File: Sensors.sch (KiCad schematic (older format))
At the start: 52 parts, among them CON1 CONSOLE, P1 CONN_02X20, P10 CBUS, P11 I2C0, P12 I2C1, P13 I2C1, P14 I2C1, P7 96B_SPI, U1 CJT1117-3.3, U2 XC6206, U3 FT230XS, U4 TXB0108PW, U5 TXS0108E, U6 PCA9306, U7 PCA9306

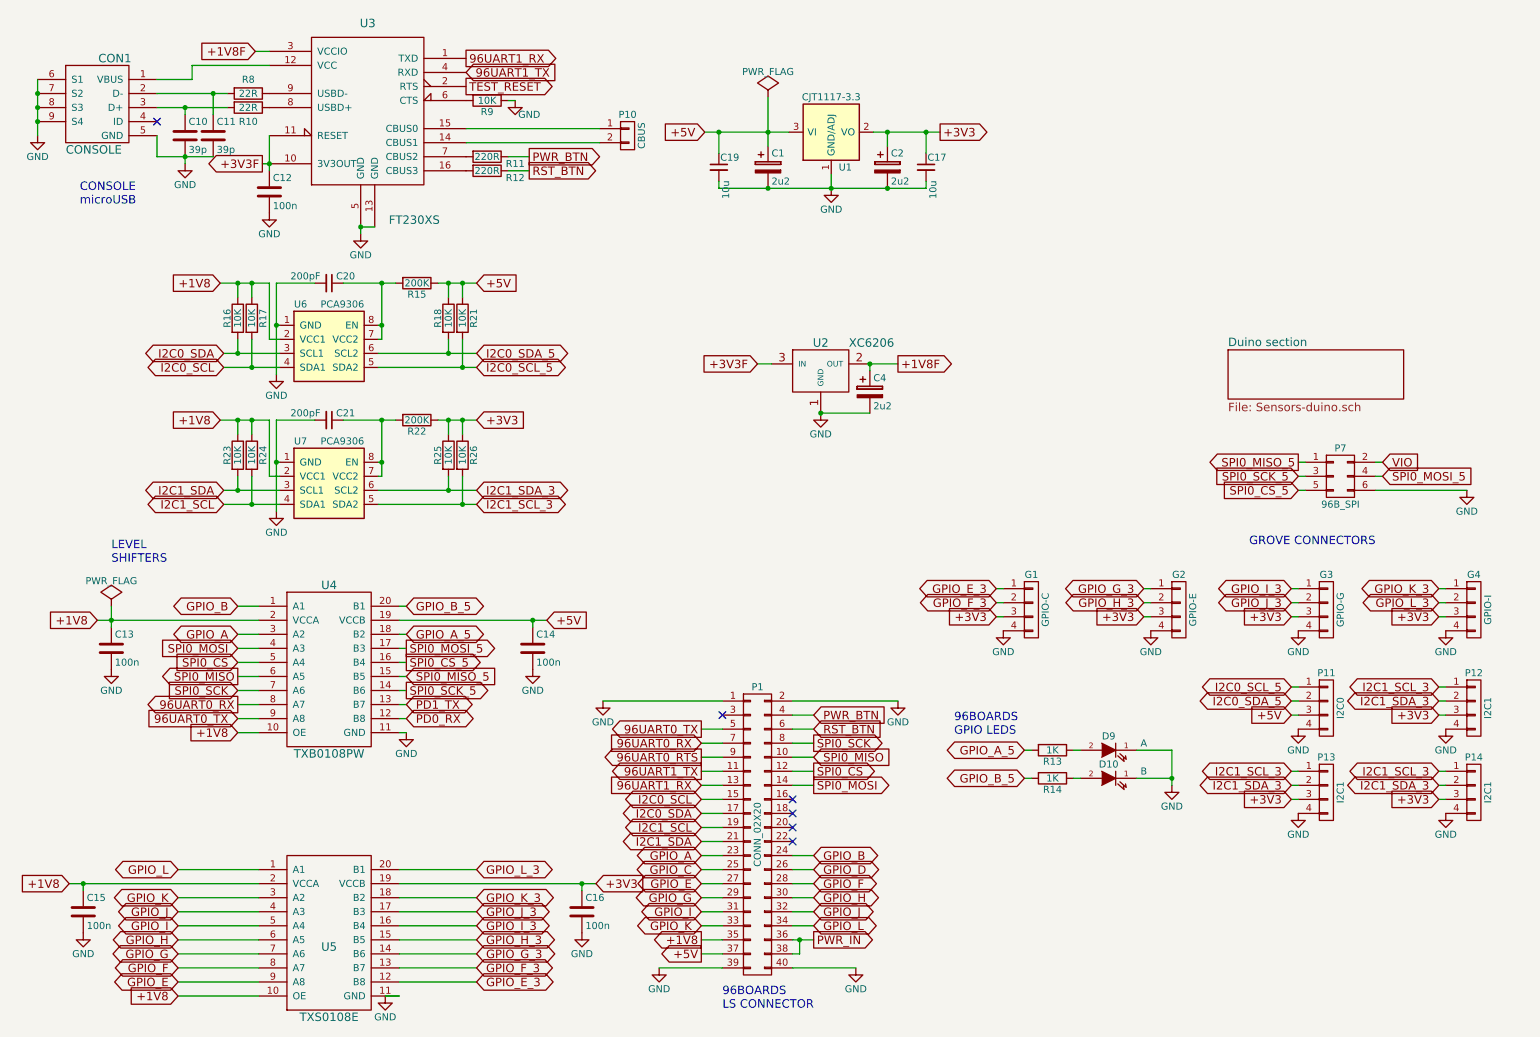
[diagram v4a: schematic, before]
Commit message: Fix missing caps on FT230X power supply
The USB power rail decoupling caps were missing for the FT230X part. Add
them back in.

Signed-off-by: Grant Likely <grant.likely@linaro.org>
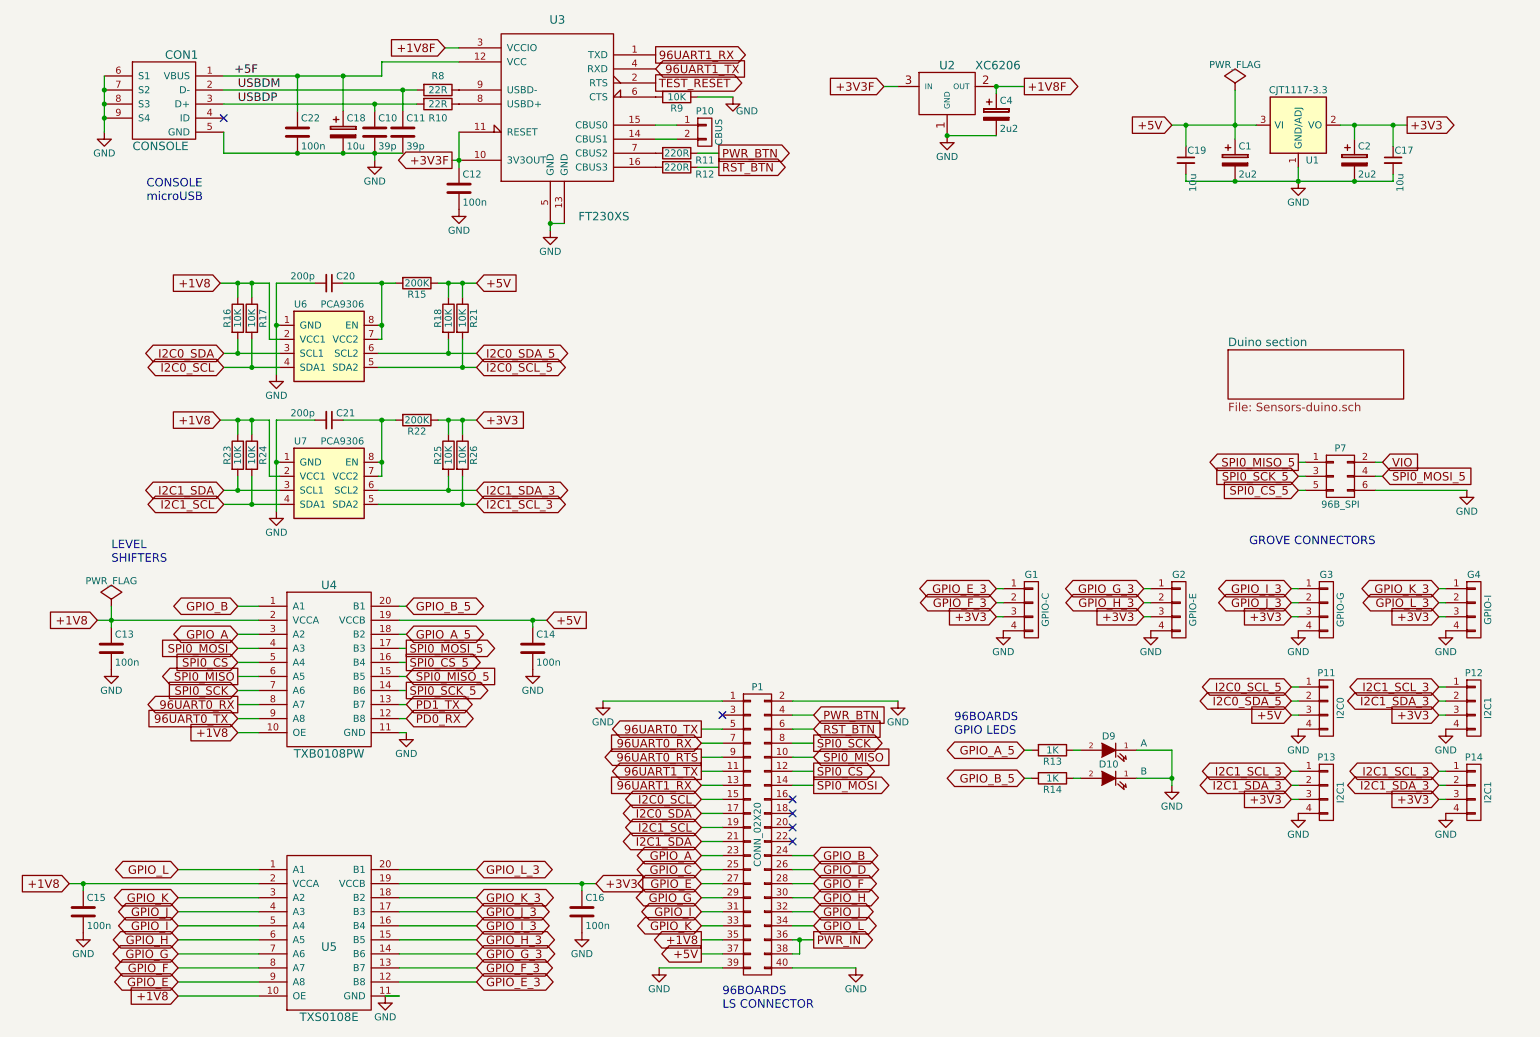
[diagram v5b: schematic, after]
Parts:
- added C18: 10u, Capacitors_SMD:C_0805, symbol CP
- added C22: 100n, Capacitors_SMD:C_0603, symbol C
- C20, C21: value 200pF -> 200p
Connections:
- net GND: now also C18.2, C22.2
- net +5F: now reaches CON1.1 (VBUS), U3.12 (VCC)
- net +5F: now also C18.1, C22.1
- net USBDM: now reaches C11.1, CON1.2 (D-), R8.2
- net USBDP: now reaches C10.1, CON1.3 (D+), R10.2
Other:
- moved on the sheet: C1, C10, C11, C12, C17, C19, C2, C4, CON1, P10, R10, R11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

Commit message: Update component part numbers
Make sure the correct part numbers are in the schematic for generating a
BOM.

Signed-off-by: Grant Likely <grant.likely@linaro.org>
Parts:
- C18: Mfr Part # CC0805KKX7R8BB225 -> CC0805KKX5R8BB106; Seeed SKU 302010148 -> 302010178
- C19: Mfr YAGEO -> Yageo
- C20, C21: value 200p -> 100p; Mfr (none) -> Yageo; Mfr Part # (none) -> CC0603JRNPO9BN101; Seeed SKU (none) -> 302010076
- C22: renamed from C17; Mfr YAGEO -> Yageo
- G1: value GPIO-C -> GROVE
- G2: value GPIO-E -> GROVE
- G3: value GPIO-G -> GROVE
- G4: value GPIO-I -> GROVE
- I2C0: renamed from P11; value I2C0 -> GROVE
- I2C1: renamed from P12; value I2C1 -> GROVE
- R15, R22: Mfr (none) -> Yageo; Mfr Part # (none) -> RC0603JR-07200KL; Seeed SKU (none) -> 301010212
- R16, R17, R18, R21, R23, R24, R25, R26: Mfr (none) -> Yageo; Mfr Part # (none) -> RC0603FR-0710KL; Seeed SKU (none) -> 301010299
- U6, U7: Mfr (none) -> TI; Mfr Part # (none) -> PCA9306DCU
- renumbered C22 to C17
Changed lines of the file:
@@
 $EndComp
 $Comp
-L CONN_01X04 P11
+L CONN_01X04 I2C0
 U 1 1 55BC070F
 P 9850 5550
-F 0 "P11" H 9850 5800 50  0000 C CNN
-F 1 "I2C0" V 9950 5550 50  0000 C CNN
+F 0 "I2C0" H 9850 5800 50  0000 C CNN
+F 1 "GROVE" V 9950 5550 50  0000 C CNN
 F 2 "Sensors:Grove_SMD_Connector" H 9850 5550 60  0001 C CNN
 F 3 "" H 9850 5550 60  0000 C CNN
@@
 $EndComp
 $Comp
-L CONN_01X04 P12
+L CONN_01X04 I2C1
 U 1 1 55BC07A4
 P 10900 5550
-F 0 "P12" H 10900 5800 50  0000 C CNN
-F 1 "I2C1" V 11000 5550 50  0000 C CNN
+F 0 "I2C1" H 10900 5800 50  0000 C CNN
+F 1 "GROVE" V 11000 5550 50  0000 C CNN
 F 2 "Sensors:Grove4P" H 10900 5550 60  0001 C CNN
 F 3 "" H 10900 5550 60  0000 C CNN
@@
 P 9850 4850
 F 0 "G3" H 9850 5100 50  0000 C CNN
-F 1 "GPIO-G" V 9950 4850 50  0000 C CNN
+F 1 "GROVE" V 9950 4850 50  0000 C CNN
 F 2 "Sensors:Grove4P" H 9850 4850 60  0001 C CNN
 F 3 "" H 9850 4850 60  0000 C CNN
@@
 P 8800 4850
 F 0 "G2" H 8800 5100 50  0000 C CNN
-F 1 "GPIO-E" V 8900 4850 50  0000 C CNN
+F 1 "GROVE" V 8900 4850 50  0000 C CNN
 F 2 "Sensors:Grove4P" H 8800 4850 60  0001 C CNN
 F 3 "" H 8800 4850 60  0000 C CNN
@@
 P 7750 4850
 F 0 "G1" H 7750 5100 50  0000 C CNN
-F 1 "GPIO-C" V 7850 4850 50  0000 C CNN
+F 1 "GROVE" V 7850 4850 50  0000 C CNN
 F 2 "Sensors:Grove_SMD_Connector" H 7750 4850 60  0001 C CNN
 F 3 "" H 7750 4850 60  0000 C CNN
@@
 F 3 "" H 8850 1650 60  0000 C CNN
 F 4 "302010178" H 8850 1650 60  0001 C CNN "Seeed SKU"
-F 5 "YAGEO" H 8850 1650 60  0001 C CNN "Mfr"
+F 5 "Yageo" H 8850 1650 60  0001 C CNN "Mfr"
 F 6 "CC0805KKX5R8BB106" H 8850 1650 60  0001 C CNN "Mfr Part #"
 	1    8850 1650
@@
 F 2 "Sensors:VSSOP-8_2.4x2.1mm_Pitch0.5mm" H 2750 2675 50  0001 C CIN
 F 3 "" H 2750 2975 60  0000 C CNN
+F 4 "TI" H 2750 2975 60  0001 C CNN "Mfr"
+F 5 "PCA9306DCU" H 2750 2975 60  0001 C CNN "Mfr Part #"
 	1    2750 2975
 	1    0    0    -1
@@
 F 2 "Sensors:R_0603_Seeed" V 3305 2525 30  0001 C CNN
 F 3 "" H 3375 2525 30  0000 C CNN
+F 4 "301010212" H 3375 2525 60  0001 C CNN "Seeed SKU"
+F 5 "Yageo" H 3375 2525 60  0001 C CNN "Mfr"
+F 6 "RC0603JR-07200KL" H 3375 2525 60  0001 C CNN "Mfr Part #"
 	1    3375 2525
 	0    1    1    0
@@
 P 2750 2525
 F 0 "C20" V 2700 2575 50  0000 L CNN
-F 1 "200p" V 2700 2250 50  0000 L CNN
+F 1 "100p" V 2700 2250 50  0000 L CNN
 F 2 "Capacitors_SMD:C_0603" H 2750 2525 60  0001 C CNN
 F 3 "" H 2750 2525 60  0000 C CNN
+F 4 "302010076" H 2750 2525 60  0001 C CNN "Seeed SKU"
+F 5 "Yageo" H 2750 2525 60  0001 C CNN "Mfr"
+F 6 "CC0603JRNPO9BN101" H 2750 2525 60  0001 C CNN "Mfr Part #"
 	1    2750 2525
 	0    1    1    0
@@
 F 2 "Sensors:R_0603_Seeed" V 3530 2775 30  0001 C CNN
 F 3 "" H 3600 2775 30  0000 C CNN
+F 4 "301010299" H 3575 -2100 60  0001 C CNN "Seeed SKU"
+F 5 "Yageo" H 3575 -2100 60  0001 C CNN "Mfr"
+F 6 "RC0603FR-0710KL" H 3575 -2100 60  0001 C CNN "Mfr Part #"
 	1    3600 2775
 	1    0    0    -1
@@
 F 2 "Sensors:R_0603_Seeed" V 3630 2775 30  0001 C CNN
 F 3 "" H 3700 2775 30  0000 C CNN
+F 4 "301010299" H 3575 -2100 60  0001 C CNN "Seeed SKU"
+F 5 "Yageo" H 3575 -2100 60  0001 C CNN "Mfr"
+F 6 "RC0603FR-0710KL" H 3575 -2100 60  0001 C CNN "Mfr Part #"
 	1    3700 2775
 	1    0    0    -1
@@
 F 2 "Sensors:R_0603_Seeed" V 2030 2775 30  0001 C CNN
 F 3 "" H 2100 2775 30  0000 C CNN
+F 4 "301010299" H 3575 -2100 60  0001 C CNN "Seeed SKU"
+F 5 "Yageo" H 3575 -2100 60  0001 C CNN "Mfr"
+F 6 "RC0603FR-0710KL" H 3575 -2100 60  0001 C CNN "Mfr Part #"
 	1    2100 2775
 	1    0    0    -1
@@
 F 2 "Sensors:R_0603_Seeed" V 2130 2775 30  0001 C CNN
 F 3 "" H 2200 2775 30  0000 C CNN
+F 4 "301010299" H 3575 -2100 60  0001 C CNN "Seeed SKU"
+F 5 "Yageo" H 3575 -2100 60  0001 C CNN "Mfr"
+F 6 "RC0603FR-0710KL" H 3575 -2100 60  0001 C CNN "Mfr Part #"
 	1    2200 2775
 	1    0    0    -1
@@
 F 2 "Sensors:VSSOP-8_2.4x2.1mm_Pitch0.5mm" H 2750 3650 50  0001 C CIN
 F 3 "" H 2750 3950 60  0000 C CNN
+F 4 "TI" H 2750 3950 60  0001 C CNN "Mfr"
+F 5 "PCA9306DCU" H 2750 3950 60  0001 C CNN "Mfr Part #"
 	1    2750 3950
 	1    0    0    -1
@@
 F 2 "Sensors:R_0603_Seeed" V 3305 3500 30  0001 C CNN
 F 3 "" H 3375 3500 30  0000 C CNN
+F 4 "301010212" H 3375 3500 60  0001 C CNN "Seeed SKU"
+F 5 "Yageo" H 3375 3500 60  0001 C CNN "Mfr"
+F 6 "RC0603JR-07200KL" H 3375 3500 60  0001 C CNN "Mfr Part #"
 	1    3375 3500
 	0    1    1    0
@@
 P 2750 3500
 F 0 "C21" V 2700 3550 50  0000 L CNN
-F 1 "200p" V 2700 3225 50  0000 L CNN
+F 1 "100p" V 2700 3225 50  0000 L CNN
 F 2 "Capacitors_SMD:C_0603" H 2750 3500 60  0001 C CNN
 F 3 "" H 2750 3500 60  0000 C CNN
+F 4 "302010076" H 2750 3500 60  0001 C CNN "Seeed SKU"
+F 5 "Yageo" H 2750 3500 60  0001 C CNN "Mfr"
+F 6 "CC0603JRNPO9BN101" H 2750 3500 60  0001 C CNN "Mfr Part #"
 	1    2750 3500
 	0    1    1    0
@@
 F 2 "Sensors:R_0603_Seeed" V 3530 3750 30  0001 C CNN
 F 3 "" H 3600 3750 30  0000 C CNN
+F 4 "301010299" H 3575 -2100 60  0001 C CNN "Seeed SKU"
+F 5 "Yageo" H 3575 -2100 60  0001 C CNN "Mfr"
+F 6 "RC0603FR-0710KL" H 3575 -2100 60  0001 C CNN "Mfr Part #"
 	1    3600 3750
 	1    0    0    -1
@@
 F 2 "Sensors:R_0603_Seeed" V 3630 3750 30  0001 C CNN
 F 3 "" H 3700 3750 30  0000 C CNN
+F 4 "301010299" H 3575 -2100 60  0001 C CNN "Seeed SKU"
+F 5 "Yageo" H 3575 -2100 60  0001 C CNN "Mfr"
+F 6 "RC0603FR-0710KL" H 3575 -2100 60  0001 C CNN "Mfr Part #"
 	1    3700 3750
 	1    0    0    -1
@@
 F 2 "Sensors:R_0603_Seeed" V 2030 3750 30  0001 C CNN
 F 3 "" H 2100 3750 30  0000 C CNN
+F 4 "301010299" H 3575 -2100 60  0001 C CNN "Seeed SKU"
+F 5 "Yageo" H 3575 -2100 60  0001 C CNN "Mfr"
+F 6 "RC0603FR-0710KL" H 3575 -2100 60  0001 C CNN "Mfr Part #"
 	1    2100 3750
 	1    0    0    -1
@@
 F 2 "Sensors:R_0603_Seeed" V 2130 3750 30  0001 C CNN
 F 3 "" H 2200 3750 30  0000 C CNN
+F 4 "301010299" H 3575 -2100 60  0001 C CNN "Seeed SKU"
+F 5 "Yageo" H 3575 -2100 60  0001 C CNN "Mfr"
+F 6 "RC0603FR-0710KL" H 3575 -2100 60  0001 C CNN "Mfr Part #"
 	1    2200 3750
 	1    0    0    -1
@@
 $EndComp
 $Comp
-L C_Small C17
+L C_Small C22
 U 1 1 565A0B7F
 P 10325 1650
-F 0 "C17" H 10335 1720 50  0000 L CNN
+F 0 "C22" H 10335 1720 50  0000 L CNN
 F 1 "10u" V 10375 1425 50  0000 L CNN
 F 2 "Capacitors_SMD:C_0805" H 10325 1650 60  0001 C CNN
 F 3 "" H 10325 1650 60  0000 C CNN
 F 4 "302010178" H 10325 1650 60  0001 C CNN "Seeed SKU"
-F 5 "YAGEO" H 10325 1650 60  0001 C CNN "Mfr"
+F 5 "Yageo" H 10325 1650 60  0001 C CNN "Mfr"
 F 6 "CC0805KKX5R8BB106" H 10325 1650 60  0001 C CNN "Mfr Part #"
 	1    10325 1650
@@
 P 10900 4850
 F 0 "G4" H 10900 5100 50  0000 C CNN
-F 1 "GPIO-I" V 11000 4850 50  0000 C CNN
+F 1 "GROVE" V 11000 4850 50  0000 C CNN
 F 2 "Sensors:Grove4P" H 10900 4850 60  0001 C CNN
 F 3 "" H 10900 4850 60  0000 C CNN
@@
 F 2 "Capacitors_SMD:C_0805" H 2888 1300 30  0001 C CNN
 F 3 "" H 2850 1450 60  0000 C CNN
-F 4 "302010148" H -2400 900 60  0001 C CNN "Seeed SKU"
+F 4 "302010178" H -2400 900 60  0001 C CNN "Seeed SKU"
 F 5 "Yageo" H -2400 900 60  0001 C CNN "Mfr"
-F 6 "CC0805KKX7R8BB225" H -2400 900 60  0001 C CNN "Mfr Part #"
+F 6 "CC0805KKX5R8BB106" H -2400 900 60  0001 C CNN "Mfr Part #"
 	1    2850 1450
 	1    0    0    -1
@@
 Connection ~ 2850 1600
 $Comp
-L C C22
+L C C17
 U 1 1 565B6698
 P 2525 1450
-F 0 "C22" H 2550 1550 50  0000 L CNN
+F 0 "C17" H 2550 1550 50  0000 L CNN
 F 1 "100n" H 2550 1350 50  0000 L CNN
 F 2 "Capacitors_SMD:C_0603" H 2563 1300 30  0001 C CNN

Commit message: Update rev C design files
Signed-off-by: Grant Likely <grant.likely@linaro.org>
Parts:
- renumbered R21 to R19
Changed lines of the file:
@@
 $EndComp
 $Comp
-L R R21
+L R R19
 U 1 1 56594717
 P 3700 2775
-F 0 "R21" V 3780 2775 50  0000 C CNN
+F 0 "R19" V 3780 2775 50  0000 C CNN
 F 1 "10K" V 3700 2775 50  0000 C CNN
 F 2 "Sensors:R_0603_Seeed" V 3630 2775 30  0001 C CNN
